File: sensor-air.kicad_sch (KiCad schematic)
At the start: 12 parts, among them J3 Conn_02x05_Odd_Even

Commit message: Adding 5V boost
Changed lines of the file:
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@@
+	(wire
+		(pts
+			(xy 154.94 93.98) (xy 173.99 93.98)
+		)
+		(stroke
+			(width 0)
+			(type default)
+		)
+	)
 	(wire
 		(pts
@@
 	(wire
 		(pts
-			(xy 154.94 93.98) (xy 173.99 93.98)
+			(xy 142.24 96.52) (xy 142.24 93.98)
 		)
 		(stroke
@@
 	(wire
 		(pts
-			(xy 142.24 96.52) (xy 142.24 93.98)
+			(xy 138.43 99.06) (xy 142.24 99.06)
 		)
 		(stroke
@@
 	(wire
 		(pts
-			(xy 138.43 99.06) (xy 142.24 99.06)
+			(xy 115.57 104.14) (xy 133.35 104.14)
 		)
 		(stroke
@@
 	(wire
 		(pts
-			(xy 115.57 104.14) (xy 133.35 104.14)
+			(xy 115.57 101.6) (xy 142.24 101.6)
 		)
 		(stroke
@@
 	(wire
 		(pts
-			(xy 115.57 101.6) (xy 142.24 101.6)
+			(xy 181.61 93.98) (xy 195.58 93.98)
 		)
 		(stroke
@@
 		(pts
 			(xy 83.82 101.6) (xy 88.9 101.6)
-		)
-		(stroke
-			(width 0)
-			(type default)
-		)
-	)
-	(wire
-		(pts
-			(xy 181.61 93.98) (xy 195.58 93.98)
 		)
 		(stroke
@@
 	)
 	(symbol
-		(lib_id "power:PWR_FLAG")
-		(at 196.85 73.66 180)
-		(unit 1)
-		(exclude_from_sim no)
-		(in_bom yes)
-		(on_board yes)
-		(dnp no)
-		(fields_autoplaced yes)
-		(property "Reference" "#FLG06"
-			(at 196.85 75.565 0)
-			(effects
-				(font
-					(size 1.27 1.27)
-				)
-				(hide yes)
-			)
-		)
-		(property "Value" "PWR_FLAG"
-			(at 196.85 78.74 0)
-			(effects
-				(font
-					(size 1.27 1.27)
-				)
-			)
-		)
-		(property "Footprint" ""
-			(at 196.85 73.66 0)
-			(effects
-				(font
-					(size 1.27 1.27)
-				)
-				(hide yes)
-			)
-		)
-		(property "Datasheet" "~"
-			(at 196.85 73.66 0)
-			(effects
-				(font
-					(size 1.27 1.27)
-				)
-				(hide yes)
-			)
-		)
-		(property "Description" "Special symbol for telling ERC where power comes from"
-			(at 196.85 73.66 0)
-			(effects
-				(font
-					(size 1.27 1.27)
-				)
-				(hide yes)
-			)
-		)
-		(pin "1"
-		)
-		(instances
-			(project ""
-				(path "/1c59de6a-87fe-4223-8898-4b0383164a31/51e979ab-bea6-4c65-a749-9f40ad447381"
-					(reference "#FLG06")
-					(unit 1)
-				)
-			)
-		)
-	)
-	(symbol
 		(lib_id "Device:R")
 		(at 137.16 106.68 270)
@@
 				(path "/1c59de6a-87fe-4223-8898-4b0383164a31/51e979ab-bea6-4c65-a749-9f40ad447381"
 					(reference "R28")
-					(unit 1)
-				)
-			)
-		)
-	)
-	(symbol
-		(lib_id "power:+5V")
-		(at 196.85 73.66 0)
-		(unit 1)
-		(exclude_from_sim no)
-		(in_bom yes)
-		(on_board yes)
-		(dnp no)
-		(fields_autoplaced yes)
-		(property "Reference" "#PWR045"
-			(at 196.85 77.47 0)
-			(effects
-				(font
-					(size 1.27 1.27)
-				)
-				(hide yes)
-			)
-		)
-		(property "Value" "+5V"
-			(at 196.85 68.58 0)
-			(effects
-				(font
-					(size 1.27 1.27)
-				)
-			)
-		)
-		(property "Footprint" ""
-			(at 196.85 73.66 0)
-			(effects
-				(font
-					(size 1.27 1.27)
-				)
-				(hide yes)
-			)
-		)
-		(property "Datasheet" ""
-			(at 196.85 73.66 0)
-			(effects
-				(font
-					(size 1.27 1.27)
-				)
-				(hide yes)
-			)
-		)
-		(property "Description" "Power symbol creates a global label with name \"+5V\""
-			(at 196.85 73.66 0)
-			(effects
-				(font
-					(size 1.27 1.27)
-				)
-				(hide yes)
-			)
-		)
-		(pin "1"
-		)
-		(instances
-			(project "roamer"
-				(path "/1c59de6a-87fe-4223-8898-4b0383164a31/51e979ab-bea6-4c65-a749-9f40ad447381"
-					(reference "#PWR045")
 					(unit 1)
 				)
@@
 				(path "/1c59de6a-87fe-4223-8898-4b0383164a31/51e979ab-bea6-4c65-a749-9f40ad447381"
 					(reference "R41")
-					(unit 1)
-				)
-			)
-		)
-	)
-	(symbol
-		(lib_id "power:+5V")
-		(at 195.58 93.98 270)
-		(unit 1)
-		(exclude_from_sim no)
-		(in_bom yes)
-		(on_board yes)
-		(dnp no)
-		(fields_autoplaced yes)
-		(property "Reference" "#PWR041"
-			(at 191.77 93.98 0)
-			(effects
-				(font
-					(size 1.27 1.27)
-				)
-				(hide yes)
-			)
-		)
-		(property "Value" "+5V"
-			(at 199.39 93.9799 90)
-			(effects
-				(font
-					(size 1.27 1.27)
-				)
-				(justify left)
-			)
-		)
-		(property "Footprint" ""
-			(at 195.58 93.98 0)
-			(effects
-				(font
-					(size 1.27 1.27)
-				)
-				(hide yes)
-			)
-		)
-		(property "Datasheet" ""
-			(at 195.58 93.98 0)
-			(effects
-				(font
-					(size 1.27 1.27)
-				)
-				(hide yes)
-			)
-		)
-		(property "Description" "Power symbol creates a global label with name \"+5V\""
-			(at 195.58 93.98 0)
-			(effects
-				(font
-					(size 1.27 1.27)
-				)
-				(hide yes)
-			)
-		)
-		(pin "1"
-		)
-		(instances
-			(project ""
-				(path "/1c59de6a-87fe-4223-8898-4b0383164a31/51e979ab-bea6-4c65-a749-9f40ad447381"
-					(reference "#PWR041")
 					(unit 1)
 				)
@@
 					(unit 1)
 				)
+			)
+		)
+	)
+	(symbol
+		(lib_id "power:+5V")
+		(at 195.58 93.98 270)
+		(unit 1)
+		(exclude_from_sim no)
+		(in_bom yes)
+		(on_board yes)
+		(dnp no)
+		(fields_autoplaced yes)
+		(property "Reference" "#PWR045"
+			(at 191.77 93.98 0)
+			(effects
+				(font
+					(size 1.27 1.27)
+				)
+				(hide yes)
+			)
+		)
+		(property "Value" "+5V"
+			(at 199.39 93.9799 90)
+			(effects
+				(font
+					(size 1.27 1.27)
+				)
+				(justify left)
+			)
+		)
+		(property "Footprint" ""
+			(at 195.58 93.98 0)
+			(effects
+				(font
+					(size 1.27 1.27)
+				)
+				(hide yes)
+			)
+		)
+		(property "Datasheet" ""
+			(at 195.58 93.98 0)
+			(effects
+				(font
+					(size 1.27 1.27)
+				)
+				(hide yes)
+			)
+		)
+		(property "Description" "Power symbol creates a global label with name \"+5V\""
+			(at 195.58 93.98 0)
+			(effects
+				(font
+					(size 1.27 1.27)
+				)
+				(hide yes)
+			)
+		)
+		(pin "1"
+		)
+		(instances
+			(project ""
+				(path "/1c59de6a-87fe-4223-8898-4b0383164a31/51e979ab-bea6-4c65-a749-9f40ad447381"
+					(reference "#PWR045")
+					(unit 1)
+				)

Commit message: Working on layout still
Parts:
- renumbered R5 to R40
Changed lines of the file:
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@@
 		(on_board yes)
 		(dnp no)
-		(property "Reference" "R5"
+		(property "Reference" "R40"
 			(at 189.484 100.584 90)
 			(effects
@@
 			(project "roamer"
 				(path "/1c59de6a-87fe-4223-8898-4b0383164a31/51e979ab-bea6-4c65-a749-9f40ad447381"
-					(reference "R5")
+					(reference "R40")
 					(unit 1)
 				)

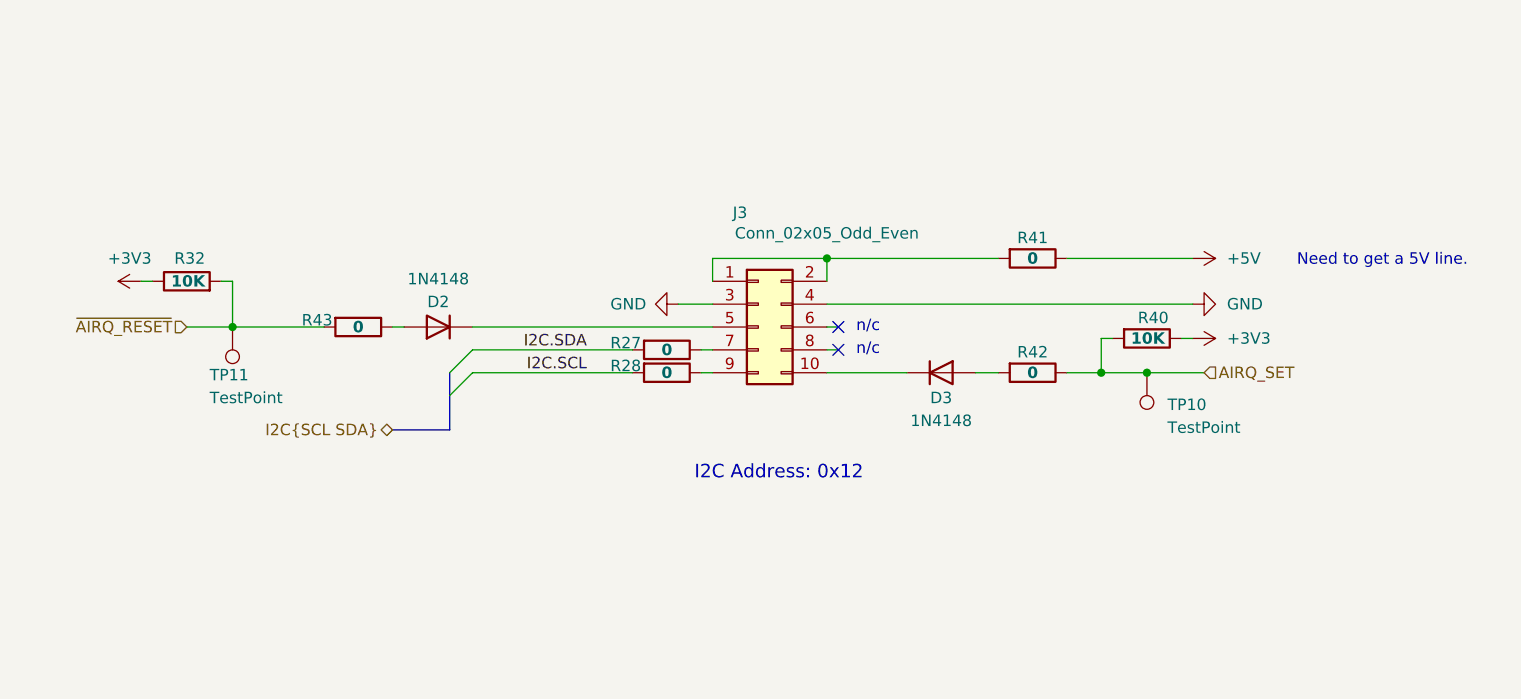
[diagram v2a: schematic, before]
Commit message: Redid board layout. Still have to add bypass caps
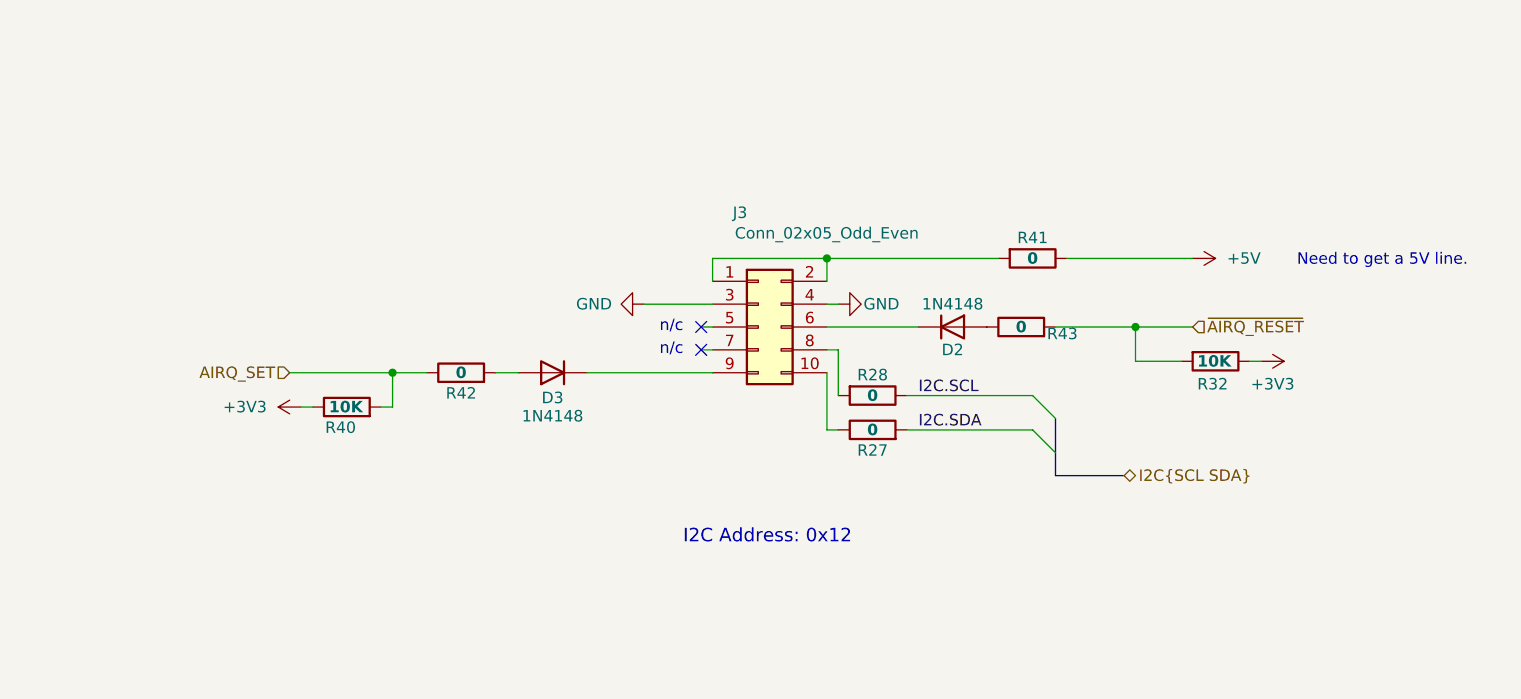
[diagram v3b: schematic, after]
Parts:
- removed TP10, TP11: TestPoint, TestPoint:TestPoint_Loop_D2.50mm_Drill1.0mm, symbol Connector:TestPoint
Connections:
- net I2C.SCL: now also R28.1; no longer R28.2
- net at J3.9 (Pin_9): now also D3.1 (K); no longer R28.1
- net at J3.10 (Pin_10): now also R27.1; no longer D3.1 (K)
- net at J3.7 (Pin_7): no longer R27.1
- net at D2.1 (K): now also J3.6 (Pin_6); no longer J3.5 (Pin_5)
- net at J3.8 (Pin_8): now also R28.2
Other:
- moved on the sheet: D3, R28, R40, R42

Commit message: Creating fab package
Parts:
- added U10: PMSA003I, symbol symbols:PMSA003I
- D2, D3: Supplier_1 Price @ Qty $0.02334 -> 0.02334; Supplier_1 Unit Price $0.10000 -> 0.10000
- J3: value Conn_02x05_Odd_Even -> Conn_02x05_Odd_Even Female; Supplier_1 Price @ Qty $0.79120 -> 0.79120; Supplier_1 Unit Price $1.35000 -> 1.35000
- R27, R28, R41, R42, R43: Supplier_1 Price @ Qty $0.00304 -> 0.00304; Supplier_1 Unit Price $0.10000 -> 0.10000
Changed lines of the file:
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@@
 			)
 		)
-		(property "Supplier_1 Unit Price" "$0.10000 "
+		(property "Supplier_1 Unit Price" "0.10000 "
 			(at 160.02 109.22 0)
 			(effects
@@
 			)
 		)
-		(property "Supplier_1 Price @ Qty" "$0.00304 "
+		(property "Supplier_1 Price @ Qty" "0.00304 "
 			(at 160.02 109.22 0)
 			(effects
@@
 			)
 		)
-		(property "Supplier_1 Unit Price" "$0.10000 "
+		(property "Supplier_1 Unit Price" "0.10000 "
 			(at 124.46 106.68 0)
 			(effects
@@
 			)
 		)
-		(property "Supplier_1 Price @ Qty" "$0.02334 "
+		(property "Supplier_1 Price @ Qty" "0.02334 "
 			(at 124.46 106.68 0)
 			(effects
@@
 			)
 		)
-		(property "Supplier_1 Unit Price" "$0.10000 "
+		(property "Supplier_1 Unit Price" "0.10000 "
 			(at 177.8 93.98 0)
 			(effects
@@
 			)
 		)
-		(property "Supplier_1 Price @ Qty" "$0.00304 "
+		(property "Supplier_1 Price @ Qty" "0.00304 "
 			(at 177.8 93.98 0)
 			(effects
@@
 			)
 		)
-		(property "Supplier_1 Unit Price" "$0.10000 "
+		(property "Supplier_1 Unit Price" "0.10000 "
 			(at 160.02 113.03 0)
 			(effects
@@
 			)
 		)
-		(property "Supplier_1 Price @ Qty" "$0.00304 "
+		(property "Supplier_1 Price @ Qty" "0.00304 "
 			(at 160.02 113.03 0)
 			(effects
@@
 			)
 		)
-		(property "Supplier_1 Unit Price" "$0.10000 "
+		(property "Supplier_1 Unit Price" "0.10000 "
 			(at 176.53 101.6 0)
 			(effects
@@
 			)
 		)
-		(property "Supplier_1 Price @ Qty" "$0.00304 "
+		(property "Supplier_1 Price @ Qty" "0.00304 "
 			(at 176.53 101.6 0)
 			(effects
@@
 	)
 	(symbol
+		(lib_id "symbols:PMSA003I")
+		(at 151.13 137.16 0)
+		(unit 1)
+		(exclude_from_sim no)
+		(in_bom yes)
+		(on_board yes)
+		(dnp no)
+		(fields_autoplaced yes)
+		(property "Reference" "U10"
+			(at 157.48 136.5249 0)
+			(effects
+				(font
+					(size 1.27 1.27)
+				)
+				(justify left)
+			)
+		)
+		(property "Value" "PMSA003I"
+			(at 157.48 138.43 0)
+			(effects
+				(font
+					(size 1.27 1.27)
+				)
+				(justify left)
+			)
+		)
+		(property "Footprint" ""
+			(at 151.13 137.16 0)
+			(effects
+				(font
+					(size 1.27 1.27)
+				)
+				(hide yes)
+			)
+		)
+		(property "Datasheet" "https://www.smart-prototyping.com/image/data/digikey/101962/PMSA003%20series%20data%20manua_English_V2.6.pdf"
+			(at 151.13 137.16 0)
+			(effects
+				(font
+					(size 1.27 1.27)
+				)
+				(hide yes)
+			)
+		)
+		(property "Description" "PM1.0 PM2.5 PM10 SENSOR PMSA003I"
+			(at 151.13 137.16 0)
+			(effects
+				(font
+					(size 1.27 1.27)
+				)
+				(hide yes)
+			)
+		)
+		(property "Mfr" "Smart Prototyping"
+			(at 151.13 137.16 0)
+			(effects
+				(font
+					(size 1.27 1.27)
+				)
+				(hide yes)
+			)
+		)
+		(property "Mfr P/N" "ZIO-101962"
+			(at 151.13 137.16 0)
+			(effects
+				(font
+					(size 1.27 1.27)
+				)
+				(hide yes)
+			)
+		)
+		(property "Supplier_1" "Digikey"
+			(at 151.13 137.16 0)
+			(effects
+				(font
+					(size 1.27 1.27)
+				)
+				(hide yes)
+			)
+		)
+		(property "Supplier_1 P/N" "3099-ZIO-101962-ND"
+			(at 151.13 137.16 0)
+			(effects
+				(font
+					(size 1.27 1.27)
+				)
+				(hide yes)
+			)
+		)
+		(property "Supplier_1 Unit Price" "35.00000"
+			(at 151.13 137.16 0)
+			(effects
+				(font
+					(size 1.27 1.27)
+				)
+				(hide yes)
+			)
+		)
+		(property "Supplier_1 Price @ Qty" "31.50000"
+			(at 151.13 137.16 0)
+			(effects
+				(font
+					(size 1.27 1.27)
+				)
+				(hide yes)
+			)
+		)
+		(property "Supplier_2" ""
+			(at 151.13 137.16 0)
+			(effects
+				(font
+					(size 1.27 1.27)
+				)
+				(hide yes)
+			)
+		)
+		(property "Supplier_2 P/N" ""
+			(at 151.13 137.16 0)
+			(effects
+				(font
+					(size 1.27 1.27)
+				)
+				(hide yes)
+			)
+		)
+		(property "Supplier_2 Unit Price" ""
+			(at 151.13 137.16 0)
+			(effects
+				(font
+					(size 1.27 1.27)
+				)
+				(hide yes)
+			)
+		)
+		(property "Supplier_2 Price @ Qty" ""
+			(at 151.13 137.16 0)
+			(effects
+				(font
+					(size 1.27 1.27)
+				)
+				(hide yes)
+			)
+		)
+		(instances
+			(project "roamer"
+				(path "/1c59de6a-87fe-4223-8898-4b0383164a31/51e979ab-bea6-4c65-a749-9f40ad447381"
+					(reference "U10")
+					(unit 1)
+				)
+			)
+		)
+	)
+	(symbol
 		(lib_id "Device:D")
 		(at 168.91 101.6 0)
@@
 			)
 		)
-		(property "Supplier_1 Unit Price" "$0.10000 "
+		(property "Supplier_1 Unit Price" "0.10000 "
 			(at 168.91 101.6 0)
 			(effects
@@
 			)
 		)
-		(property "Supplier_1 Price @ Qty" "$0.02334 "
+		(property "Supplier_1 Price @ Qty" "0.02334 "
 			(at 168.91 101.6 0)
 			(effects
@@
 			)
 		)
-		(property "Supplier_1 Unit Price" "$0.10000 "
+		(property "Supplier_1 Unit Price" "0.10000 "
 			(at 114.3 106.68 0)
 			(effects
@@
 			)
 		)
-		(property "Supplier_1 Price @ Qty" "$0.00304 "
+		(property "Supplier_1 Price @ Qty" "0.00304 "
 			(at 114.3 106.68 0)
 			(effects
@@
 			)
 		)
-		(property "Value" "Conn_02x05_Odd_Even"
+		(property "Value" "Conn_02x05_Odd_Even Female"
 			(at 154.94 91.186 0)
 			(effects
@@
 			)
 		)
-		(property "Supplier_1 Unit Price" "$1.35000 "
+		(property "Supplier_1 Unit Price" "1.35000 "
 			(at 147.32 101.6 0)
 			(effects
@@
 			)
 		)
-		(property "Supplier_1 Price @ Qty" "$0.79120 "
+		(property "Supplier_1 Price @ Qty" "0.79120 "
 			(at 147.32 101.6 0)
 			(effects
